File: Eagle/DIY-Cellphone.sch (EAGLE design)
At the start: 66 parts, among them IC1 MEGA1284, J1 ISP, U1 MCP73831, X1 BU-SMA-V, X3 CCM03-3002 R102

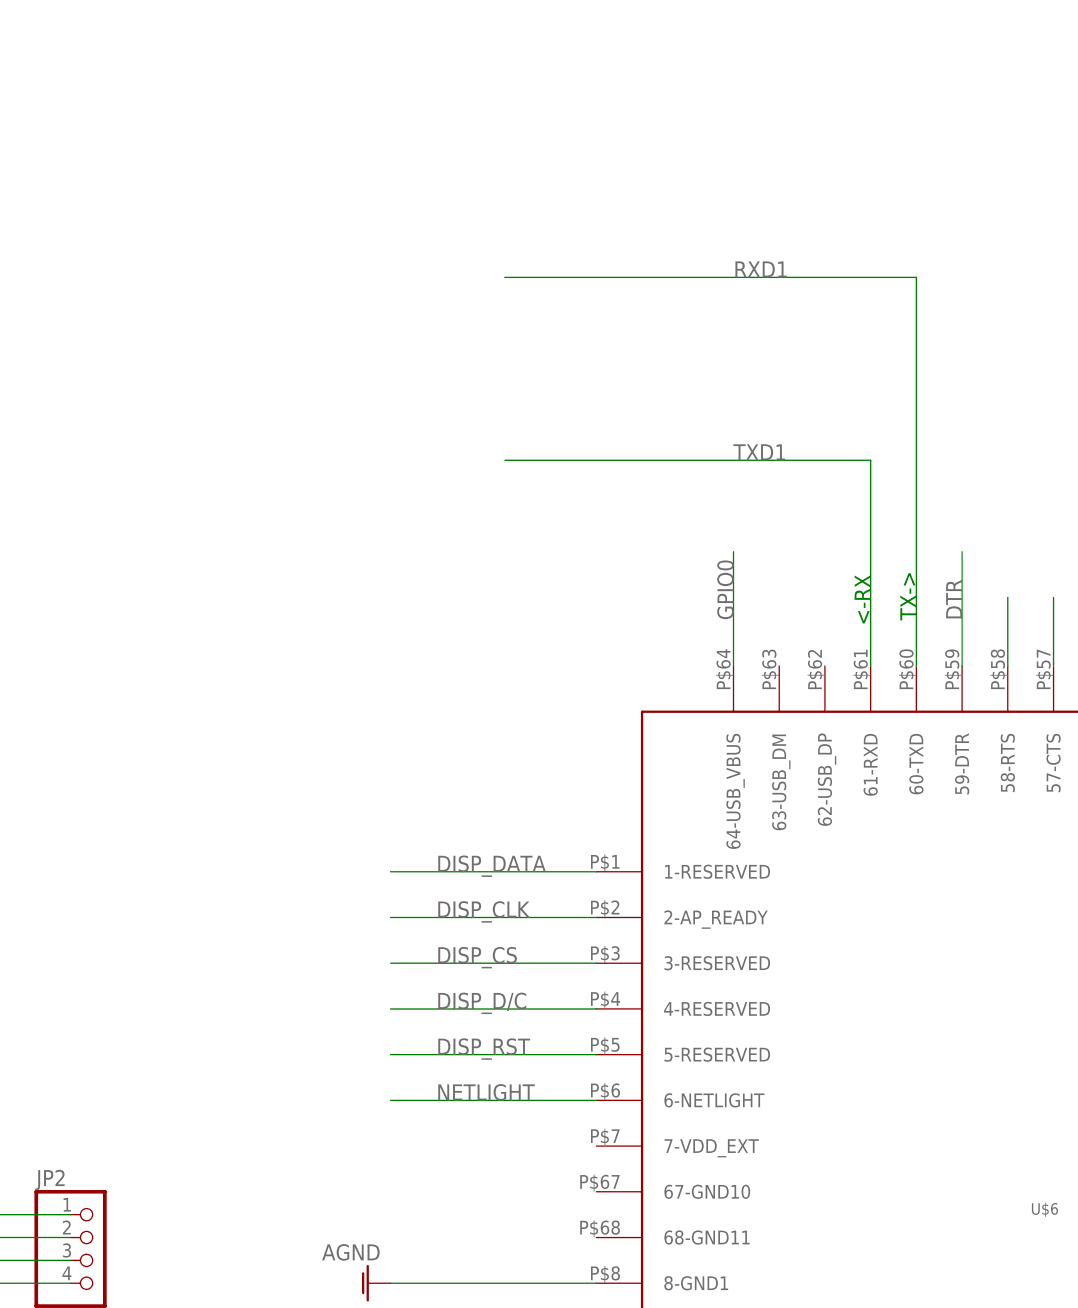
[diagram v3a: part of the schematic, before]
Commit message: Add TXB0104 level shifter.
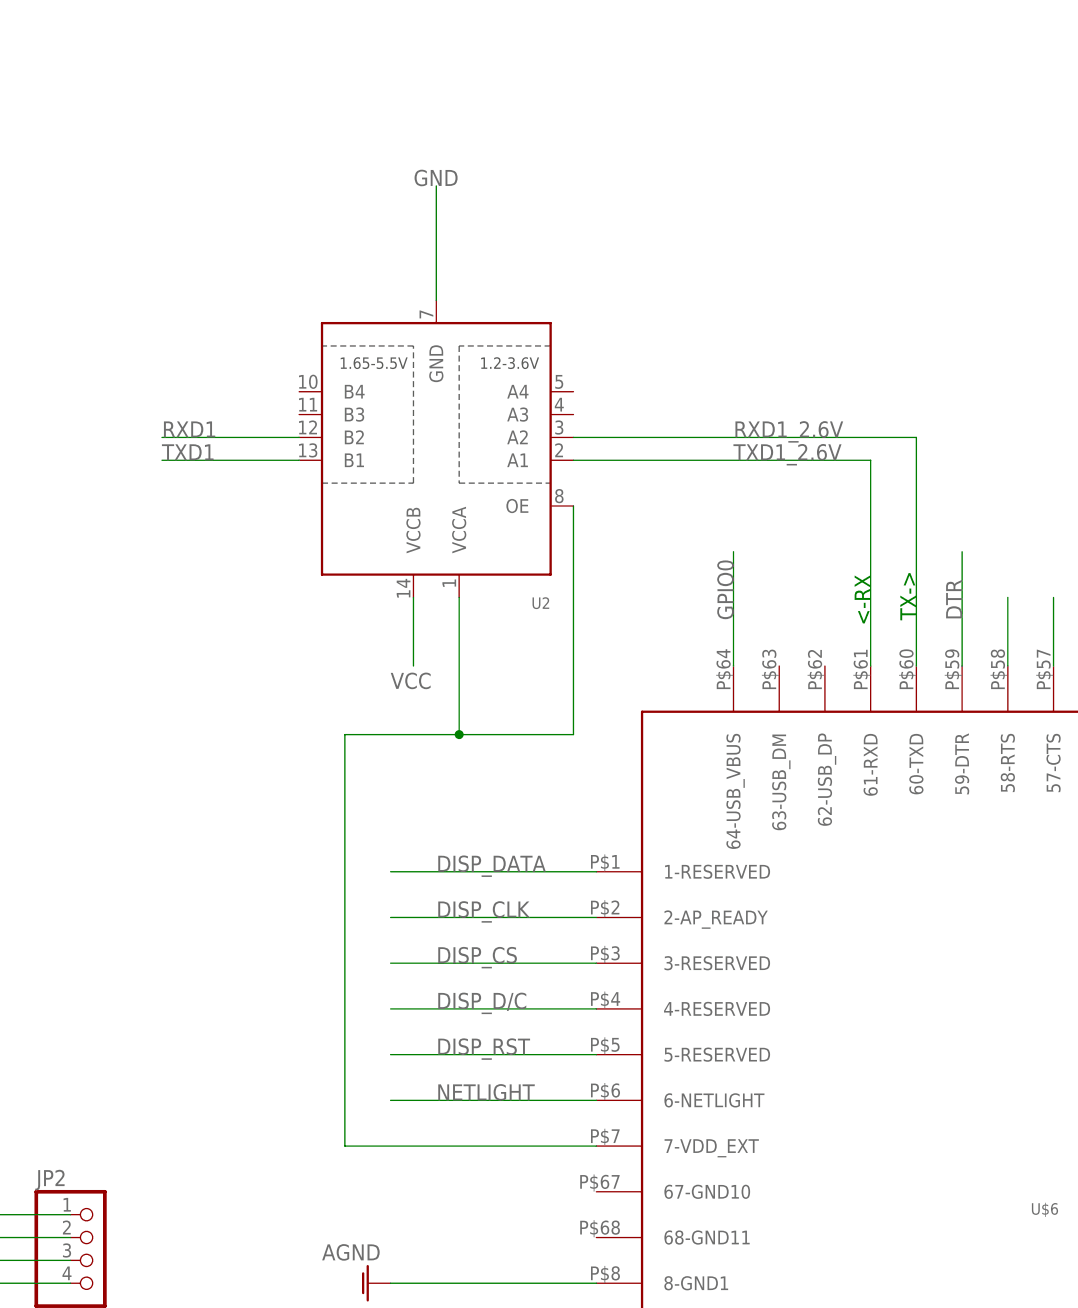
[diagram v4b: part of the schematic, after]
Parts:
- added U2: (no value), SparkFun-DigitalIC:TXB0104PWRSOIC14
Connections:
- new net N$2: U$6.7-VDD_EXT, U2.OE, U2.VCCA
- new net RXD1_2.6V: U$6.60-TXD, U2.A2
- new net TXD1_2.6V: U$6.61-RXD, U2.A1
- net GND: now also U2.GND
- net RXD1: now also U2.B2; no longer U$6.60-TXD
- net TXD1: now also U2.B1; no longer U$6.61-RXD
- net VCC: now also U2.VCCB
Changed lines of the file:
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@@
 <layer number="54" name="bGND_GNDA" color="7" fill="1" visible="no" active="no"/>
 <layer number="56" name="wert" color="7" fill="1" visible="no" active="no"/>
+<layer number="57" name="tCAD" color="7" fill="1" visible="no" active="no"/>
 <layer number="91" name="Nets" color="2" fill="1" visible="yes" active="yes"/>
 <layer number="92" name="Busses" color="1" fill="1" visible="yes" active="yes"/>
@@
 <layer number="97" name="Info" color="7" fill="1" visible="no" active="yes"/>
 <layer number="98" name="Guide" color="6" fill="1" visible="no" active="yes"/>
+<layer number="99" name="SpiceOrder" color="7" fill="1" visible="yes" active="yes"/>
 <layer number="100" name="Muster" color="7" fill="1" visible="no" active="yes"/>
 <layer number="101" name="Patch_Top" color="7" fill="1" visible="no" active="yes"/>
@@
 <layer number="106" name="bPlate" color="7" fill="1" visible="no" active="yes"/>
 <layer number="107" name="Crop" color="7" fill="1" visible="no" active="yes"/>
+<layer number="108" name="tplace-old" color="10" fill="1" visible="yes" active="yes"/>
+<layer number="109" name="ref-old" color="11" fill="1" visible="yes" active="yes"/>
+<layer number="110" name="fp0" color="7" fill="1" visible="yes" active="yes"/>
+<layer number="111" name="LPC17xx" color="7" fill="1" visible="yes" active="yes"/>
+<layer number="112" name="tSilk" color="7" fill="1" visible="yes" active="yes"/>
+<layer number="113" name="IDFDebug" color="7" fill="1" visible="yes" active="yes"/>
 <layer number="116" name="Patch_BOT" color="7" fill="1" visible="no" active="yes"/>
 <layer number="121" name="_tsilk" color="7" fill="1" visible="no" active="yes"/>
 <layer number="122" name="_bsilk" color="7" fill="1" visible="no" active="yes"/>
+<layer number="123" name="tTestmark" color="7" fill="1" visible="yes" active="yes"/>
+<layer number="124" name="bTestmark" color="7" fill="1" visible="yes" active="yes"/>
 <layer number="125" name="_tNames" color="7" fill="1" visible="no" active="yes"/>
+<layer number="126" name="_bNames" color="7" fill="1" visible="yes" active="yes"/>
+<layer number="127" name="_tValues" color="7" fill="1" visible="yes" active="yes"/>
+<layer number="128" name="_bValues" color="7" fill="1" visible="yes" active="yes"/>
+<layer number="131" name="tAdjust" color="7" fill="1" visible="yes" active="yes"/>
+<layer number="132" name="bAdjust" color="7" fill="1" visible="yes" active="yes"/>
 <layer number="144" name="Drill_legend" color="7" fill="1" visible="no" active="yes"/>
+<layer number="150" name="Notes" color="7" fill="1" visible="yes" active="yes"/>
 <layer number="151" name="HeatSink" color="7" fill="1" visible="no" active="yes"/>
+<layer number="152" name="_bDocu" color="7" fill="1" visible="yes" active="yes"/>
+<layer number="153" name="FabDoc1" color="7" fill="1" visible="yes" active="yes"/>
+<layer number="154" name="FabDoc2" color="7" fill="1" visible="yes" active="yes"/>
+<layer number="155" name="FabDoc3" color="7" fill="1" visible="yes" active="yes"/>
+<layer number="199" name="Contour" color="7" fill="1" visible="yes" active="yes"/>
 <layer number="200" name="200bmp" color="1" fill="10" visible="no" active="no"/>
 <layer number="201" name="201bmp" color="7" fill="1" visible="no" active="yes"/>
@@
 <layer number="223" name="223bmp" color="24" fill="1" visible="no" active="yes"/>
 <layer number="224" name="224bmp" color="25" fill="1" visible="no" active="yes"/>
+<layer number="248" name="Housing" color="7" fill="1" visible="yes" active="yes"/>
+<layer number="249" name="Edge" color="7" fill="1" visible="yes" active="yes"/>
 <layer number="250" name="Descript" color="3" fill="1" visible="no" active="no"/>
 <layer number="251" name="SMDround" color="12" fill="11" visible="no" active="no"/>
@@
 <part name="JP2" library="pinhead" deviceset="PINHD-1X4" device=""/>
 <part name="U$6" library="cellphone" deviceset="UC15" device=""/>
+<part name="U2" library="SparkFun-DigitalIC" deviceset="TXB0104PWR" device="SOIC14"/>
 </parts>
 <sheets>
@@
 <instance part="JP2" gate="A" x="38.1" y="81.28"/>
 <instance part="U$6" gate="G$1" x="147.32" y="91.44"/>
+<instance part="U2" gate="G$1" x="76.2" y="172.72" rot="R180"/>
 </instances>
 <busses>
@@
 <wire x1="73.66" y1="248.92" x2="99.06" y2="248.92" width="0.1524" layer="91"/>
 <label x="99.06" y="248.92" size="1.778" layer="95" rot="MR0"/>
+</segment>
+<segment>
+<pinref part="U2" gate="G$1" pin="VCCB"/>
+<wire x1="73.66" y1="154.94" x2="73.66" y2="147.32" width="0.1524" layer="91"/>
+<label x="71.12" y="144.78" size="1.778" layer="95"/>
 </segment>
 </net>
@@
 <label x="99.06" y="243.84" size="1.778" layer="95" rot="MR0"/>
 </segment>
+<segment>
+<pinref part="U2" gate="G$1" pin="GND"/>
+<wire x1="76.2" y1="187.96" x2="76.2" y2="200.66" width="0.1524" layer="91"/>
+<label x="73.66" y="200.66" size="1.778" layer="95"/>
+</segment>
 </net>
 <net name="DISP_DATA" class="0">
@@
 </segment>
 <segment>
-<wire x1="129.54" y1="147.32" x2="129.54" y2="190.5" width="0.1524" layer="91"/>
-<wire x1="83.82" y1="190.5" x2="129.54" y2="190.5" width="0.1524" layer="91"/>
-<label x="109.22" y="190.5" size="1.778" layer="95"/>
-<pinref part="U$6" gate="G$1" pin="60-TXD"/>
-</segment>
-<segment>
 <pinref part="SJ2" gate="G$1" pin="3"/>
 <wire x1="48.26" y1="-7.62" x2="55.88" y2="-7.62" width="0.1524" layer="91"/>
 <label x="55.88" y="-7.62" size="1.778" layer="95" rot="MR0"/>
 </segment>
+<segment>
+<pinref part="U2" gate="G$1" pin="B2"/>
+<wire x1="60.96" y1="172.72" x2="45.72" y2="172.72" width="0.1524" layer="91"/>
+<label x="45.72" y="172.72" size="1.778" layer="95"/>
+</segment>
 </net>
 <net name="TXD1" class="0">
@@
 </segment>
 <segment>
-<wire x1="124.46" y1="147.32" x2="124.46" y2="170.18" width="0.1524" layer="91"/>
-<wire x1="124.46" y1="170.18" x2="83.82" y2="170.18" width="0.1524" layer="91"/>
-<label x="109.22" y="170.18" size="1.778" layer="95"/>
-<pinref part="U$6" gate="G$1" pin="61-RXD"/>
-</segment>
-<segment>
 <pinref part="SJ1" gate="G$1" pin="3"/>
 <wire x1="17.78" y1="-5.08" x2="25.4" y2="-5.08" width="0.1524" layer="91"/>
 <label x="25.4" y="-5.08" size="1.778" layer="95" rot="MR0"/>
+</segment>
+<segment>
+<pinref part="U2" gate="G$1" pin="B1"/>
+<wire x1="60.96" y1="170.18" x2="45.72" y2="170.18" width="0.1524" layer="91"/>
+<label x="45.72" y="170.18" size="1.778" layer="95"/>
 </segment>
 </net>
@@
 </segment>
 </net>
+<net name="RXD1_2.6V" class="0">
+<segment>
+<wire x1="129.54" y1="147.32" x2="129.54" y2="172.72" width="0.1524" layer="91"/>
+<wire x1="91.44" y1="172.72" x2="129.54" y2="172.72" width="0.1524" layer="91"/>
+<label x="109.22" y="172.72" size="1.778" layer="95"/>
+<pinref part="U$6" gate="G$1" pin="60-TXD"/>
+<pinref part="U2" gate="G$1" pin="A2"/>
+</segment>
+</net>
+<net name="TXD1_2.6V" class="0">
+<segment>
+<wire x1="124.46" y1="147.32" x2="124.46" y2="170.18" width="0.1524" layer="91"/>
+<wire x1="124.46" y1="170.18" x2="91.44" y2="170.18" width="0.1524" layer="91"/>
+<label x="109.22" y="170.18" size="1.778" layer="95"/>
+<pinref part="U$6" gate="G$1" pin="61-RXD"/>
+<pinref part="U2" gate="G$1" pin="A1"/>
+</segment>
+</net>
+<net name="N$2" class="0">
+<segment>
+<pinref part="U$6" gate="G$1" pin="7-VDD_EXT"/>
+<wire x1="93.98" y1="93.98" x2="66.04" y2="93.98" width="0.1524" layer="91"/>
+<wire x1="66.04" y1="93.98" x2="66.04" y2="139.7" width="0.1524" layer="91"/>
+<pinref part="U2" gate="G$1" pin="VCCA"/>
+<wire x1="66.04" y1="139.7" x2="78.74" y2="139.7" width="0.1524" layer="91"/>
+<wire x1="78.74" y1="139.7" x2="78.74" y2="154.94" width="0.1524" layer="91"/>
+<pinref part="U2" gate="G$1" pin="OE"/>
+<wire x1="91.44" y1="165.1" x2="91.44" y2="139.7" width="0.1524" layer="91"/>
+<wire x1="91.44" y1="139.7" x2="78.74" y2="139.7" width="0.1524" layer="91"/>
+<junction x="78.74" y="139.7"/>
+</segment>
+</net>
